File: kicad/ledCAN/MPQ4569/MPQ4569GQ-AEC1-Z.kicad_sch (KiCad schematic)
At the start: 10 parts

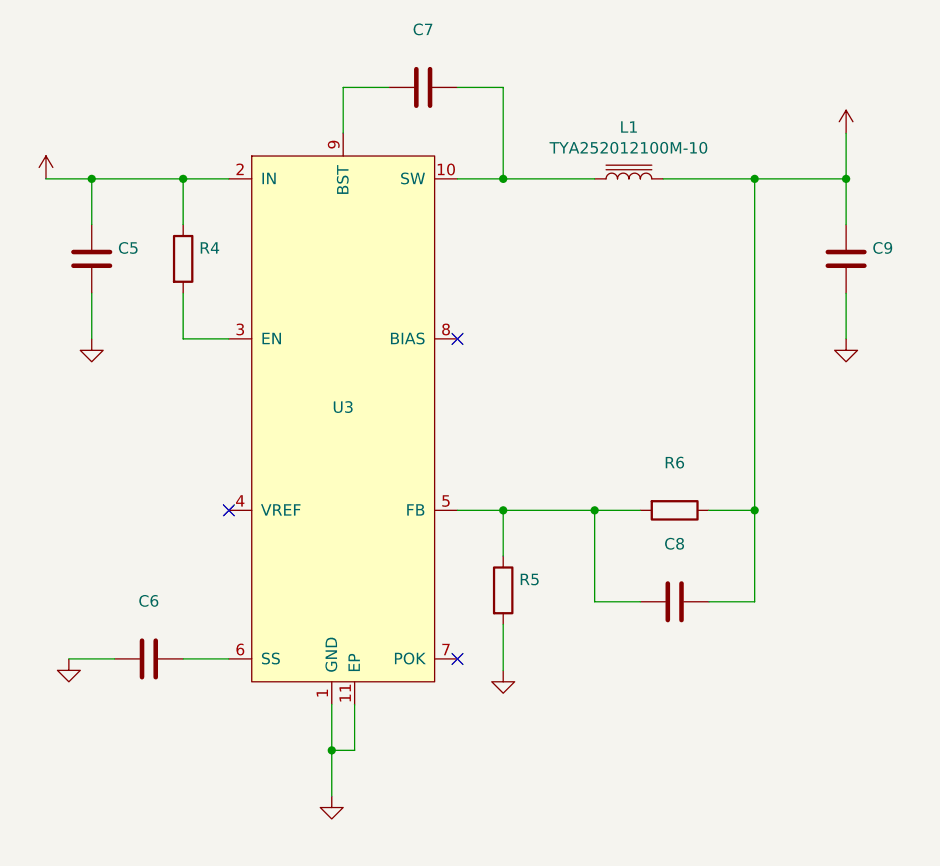
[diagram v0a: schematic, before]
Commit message: Update page settings
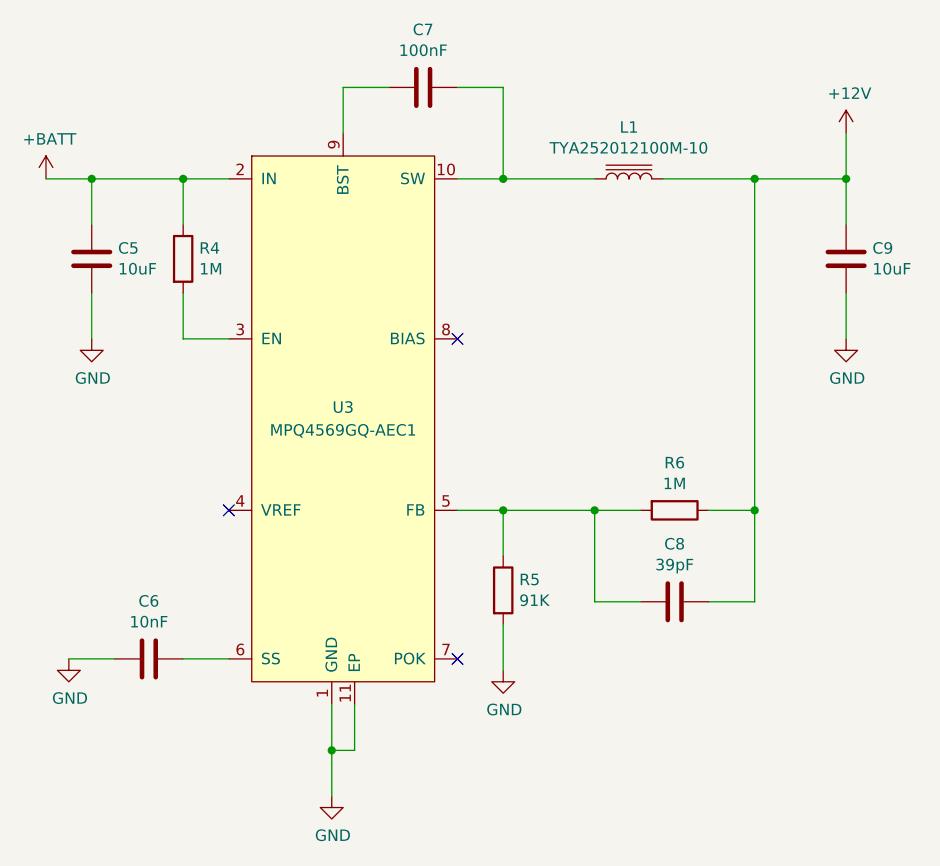
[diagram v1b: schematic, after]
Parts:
- C5: value (none) -> 10uF; footprint (none) -> Capacitor_SMD:C_1210_3225Metric
- C6: value (none) -> 10nF; footprint (none) -> Capacitor_SMD:C_0603_1608Metric
- C7: value (none) -> 100nF; footprint (none) -> Capacitor_SMD:C_0603_1608Metric
- C8: value (none) -> 39pF; footprint (none) -> Capacitor_SMD:C_0603_1608Metric
- C9: value (none) -> 10uF; footprint (none) -> Capacitor_SMD:C_0805_2012Metric
- R4, R6: value (none) -> 1M; footprint (none) -> Resistor_SMD:R_0603_1608Metric
- R5: value (none) -> 91K; footprint (none) -> Resistor_SMD:R_0603_1608Metric
- U3: value (none) -> MPQ4569GQ-AEC1; footprint (none) -> QFN-10-1EP_3x3mm_P0.5mm_EP1.7x2.5mm:QFN-10-1EP_3x3mm_P0.5mm_EP1.7x2.5mm
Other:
- company: DANCHOUZHOU -> City Science Lab @ Taipei Tech /a cooperation with the MIT Media Lab
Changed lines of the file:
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@@
   (title_block
     (title "Multi purpose power converter module with CAN bus interface")
-    (date "2021-08-31")
-    (rev "1.1")
-    (company "DANCHOUZHOU")
-    (comment 1 "City Science - MIT Media Lab")
-    (comment 2 "danchouzhou@gmail.com")
+    (date "2022-09-07")
+    (rev "0.1")
+    (company "City Science Lab @ Taipei Tech /a cooperation with the MIT Media Lab")
+    (comment 1 "DANCHOUZHOU")
+    (comment 2 "https://github.com/danchouzhou")
+    (comment 3 "danchouzhou@gmail.com")
   )
   (junction (at 138.43 138.43) (diameter 0) (color 0 0 0 0)
@@
     (in_bom yes) (on_board yes)
     (property "Reference" "U3" (id 0) (at 139.7 100.33 0))
-    (property "Value" "" (id 1) (at 139.7 102.87 0))
-    (property "Footprint" "" (id 2) (at 139.7 68.58 0)
+    (property "Value" "MPQ4569GQ-AEC1" (id 1) (at 139.7 102.87 0))
+    (property "Footprint" "QFN-10-1EP_3x3mm_P0.5mm_EP1.7x2.5mm:QFN-10-1EP_3x3mm_P0.5mm_EP1.7x2.5mm" (id 2) (at 139.7 68.58 0)
       (effects (font (size 1.27 1.27)) hide)
     )
@@
       (effects (font (size 1.27 1.27)) (justify left))
     )
-    (property "Value" "" (id 1) (at 123.698 84.963 0)
-      (effects (font (size 1.27 1.27)) (justify left))
-    )
-    (property "Footprint" "" (id 2) (at 120.142 83.82 90)
+    (property "Value" "1M" (id 1) (at 123.698 84.963 0)
+      (effects (font (size 1.27 1.27)) (justify left))
+    )
+    (property "Footprint" "Resistor_SMD:R_0603_1608Metric" (id 2) (at 120.142 83.82 90)
       (effects (font (size 1.27 1.27)) hide)
     )
@@
     (in_bom yes) (on_board yes)
     (property "Reference" "C6" (id 0) (at 118.11 121.8692 90))
-    (property "Value" "" (id 1) (at 118.11 124.1806 90))
-    (property "Footprint" "" (id 2) (at 114.3 129.2352 0)
+    (property "Value" "10nF" (id 1) (at 118.11 124.1806 90))
+    (property "Footprint" "Capacitor_SMD:C_0603_1608Metric" (id 2) (at 114.3 129.2352 0)
       (effects (font (size 1.27 1.27)) hide)
     )
@@
       (effects (font (size 1.27 1.27)) hide)
     )
-    (property "Value" "" (id 1) (at 109.347 132.6642 0))
+    (property "Value" "GND" (id 1) (at 109.347 132.6642 0))
     (property "Footprint" "" (id 2) (at 109.22 128.27 0)
       (effects (font (size 1.27 1.27)) hide)
@@
       (effects (font (size 1.27 1.27)) hide)
     )
-    (property "Value" "" (id 1) (at 138.557 147.9042 0))
+    (property "Value" "GND" (id 1) (at 138.557 147.9042 0))
     (property "Footprint" "" (id 2) (at 138.43 143.51 0)
       (effects (font (size 1.27 1.27)) hide)
@@
       (effects (font (size 1.27 1.27)) (justify left))
     )
-    (property "Value" "" (id 1) (at 198.501 84.963 0)
-      (effects (font (size 1.27 1.27)) (justify left))
-    )
-    (property "Footprint" "" (id 2) (at 196.5452 87.63 0)
+    (property "Value" "10uF" (id 1) (at 198.501 84.963 0)
+      (effects (font (size 1.27 1.27)) (justify left))
+    )
+    (property "Footprint" "Capacitor_SMD:C_0805_2012Metric" (id 2) (at 196.5452 87.63 0)
       (effects (font (size 1.27 1.27)) hide)
     )
@@
       (effects (font (size 1.27 1.27)) hide)
     )
-    (property "Value" "" (id 1) (at 195.707 97.1042 0))
+    (property "Value" "GND" (id 1) (at 195.707 97.1042 0))
     (property "Footprint" "" (id 2) (at 195.58 92.71 0)
       (effects (font (size 1.27 1.27)) hide)
@@
       (effects (font (size 1.27 1.27)) hide)
     )
-    (property "Value" "" (id 1) (at 195.961 65.4558 0))
+    (property "Value" "+12V" (id 1) (at 195.961 65.4558 0))
     (property "Footprint" "" (id 2) (at 195.58 69.85 0)
       (effects (font (size 1.27 1.27)) hide)
@@
       (effects (font (size 1.27 1.27)) (justify left))
     )
-    (property "Value" "" (id 1) (at 114.681 84.963 0)
-      (effects (font (size 1.27 1.27)) (justify left))
-    )
-    (property "Footprint" "" (id 2) (at 112.7252 87.63 0)
+    (property "Value" "10uF" (id 1) (at 114.681 84.963 0)
+      (effects (font (size 1.27 1.27)) (justify left))
+    )
+    (property "Footprint" "Capacitor_SMD:C_1210_3225Metric" (id 2) (at 112.7252 87.63 0)
       (effects (font (size 1.27 1.27)) hide)
     )
@@
       (effects (font (size 1.27 1.27)) hide)
     )
-    (property "Value" "" (id 1) (at 107.061 70.5358 0))
+    (property "Value" "+BATT" (id 1) (at 107.061 70.5358 0))
     (property "Footprint" "" (id 2) (at 106.68 74.93 0)
       (effects (font (size 1.27 1.27)) hide)
@@
       (effects (font (size 1.27 1.27)) hide)
     )
-    (property "Value" "" (id 1) (at 111.887 97.1042 0))
+    (property "Value" "GND" (id 1) (at 111.887 97.1042 0))
     (property "Footprint" "" (id 2) (at 111.76 92.71 0)
       (effects (font (size 1.27 1.27)) hide)
@@
     (in_bom yes) (on_board yes)
     (property "Reference" "C7" (id 0) (at 148.59 58.3692 90))
-    (property "Value" "" (id 1) (at 148.59 60.6806 90))
-    (property "Footprint" "" (id 2) (at 144.78 65.7352 0)
+    (property "Value" "100nF" (id 1) (at 148.59 60.6806 90))
+    (property "Footprint" "Capacitor_SMD:C_0603_1608Metric" (id 2) (at 144.78 65.7352 0)
       (effects (font (size 1.27 1.27)) hide)
     )
@@
     (in_bom yes) (on_board yes)
     (property "Reference" "R6" (id 0) (at 176.53 106.5022 90))
-    (property "Value" "" (id 1) (at 176.53 108.8136 90))
-    (property "Footprint" "" (id 2) (at 176.53 109.982 90)
+    (property "Value" "1M" (id 1) (at 176.53 108.8136 90))
+    (property "Footprint" "Resistor_SMD:R_0603_1608Metric" (id 2) (at 176.53 109.982 90)
       (effects (font (size 1.27 1.27)) hide)
     )
@@
     (in_bom yes) (on_board yes)
     (property "Reference" "C8" (id 0) (at 176.53 115.5192 90))
-    (property "Value" "" (id 1) (at 176.53 117.8306 90))
-    (property "Footprint" "" (id 2) (at 172.72 122.8852 0)
+    (property "Value" "39pF" (id 1) (at 176.53 117.8306 90))
+    (property "Footprint" "Capacitor_SMD:C_0603_1608Metric" (id 2) (at 172.72 122.8852 0)
       (effects (font (size 1.27 1.27)) hide)
     )
@@
       (effects (font (size 1.27 1.27)) (justify left))
     )
-    (property "Value" "" (id 1) (at 159.258 121.793 0)
-      (effects (font (size 1.27 1.27)) (justify left))
-    )
-    (property "Footprint" "" (id 2) (at 155.702 120.65 90)
+    (property "Value" "91K" (id 1) (at 159.258 121.793 0)
+      (effects (font (size 1.27 1.27)) (justify left))
+    )
+    (property "Footprint" "Resistor_SMD:R_0603_1608Metric" (id 2) (at 155.702 120.65 90)
       (effects (font (size 1.27 1.27)) hide)
     )
@@
       (effects (font (size 1.27 1.27)) hide)
     )
-    (property "Value" "" (id 1) (at 157.607 133.9342 0))
+    (property "Value" "GND" (id 1) (at 157.607 133.9342 0))
     (property "Footprint" "" (id 2) (at 157.48 129.54 0)
       (effects (font (size 1.27 1.27)) hide)
